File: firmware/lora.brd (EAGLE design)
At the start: 20.2 x 71.1 mm, 24 parts, among them J1 SWD_PTH_SHROUD, X1 SMA-142-0701-801/806

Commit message: some nudging
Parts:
- removed U$5: BUS-SMA, Ava:BUS-SMA
- moved X1 5.38 mm to (10.2, 0.76)
- moved J1 1.27 mm to (2.54, 55.9)
- moved U$1 1.27 mm to (10.2, 34.3)
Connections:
- net GND: no longer U$5.2, U$5.3, U$5.4, U$5.5
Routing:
- net RST: track 38.0 -> 27.6 mm
- net SWCLK: track 25.9 -> 20.3 mm
- net N$2: track 8.12 -> 12.9 mm
- net GND: track 171.4 -> 168.1 mm
- net SWDAT: track 23.3 -> 20.6 mm
- net N$4: track 57.7 -> 56.5 mm
- net +3V3: track 100.1 -> 99.5 mm
- net GPIO3: track 21.3 -> 20.8 mm
- added copper zone on layer 1, net GND

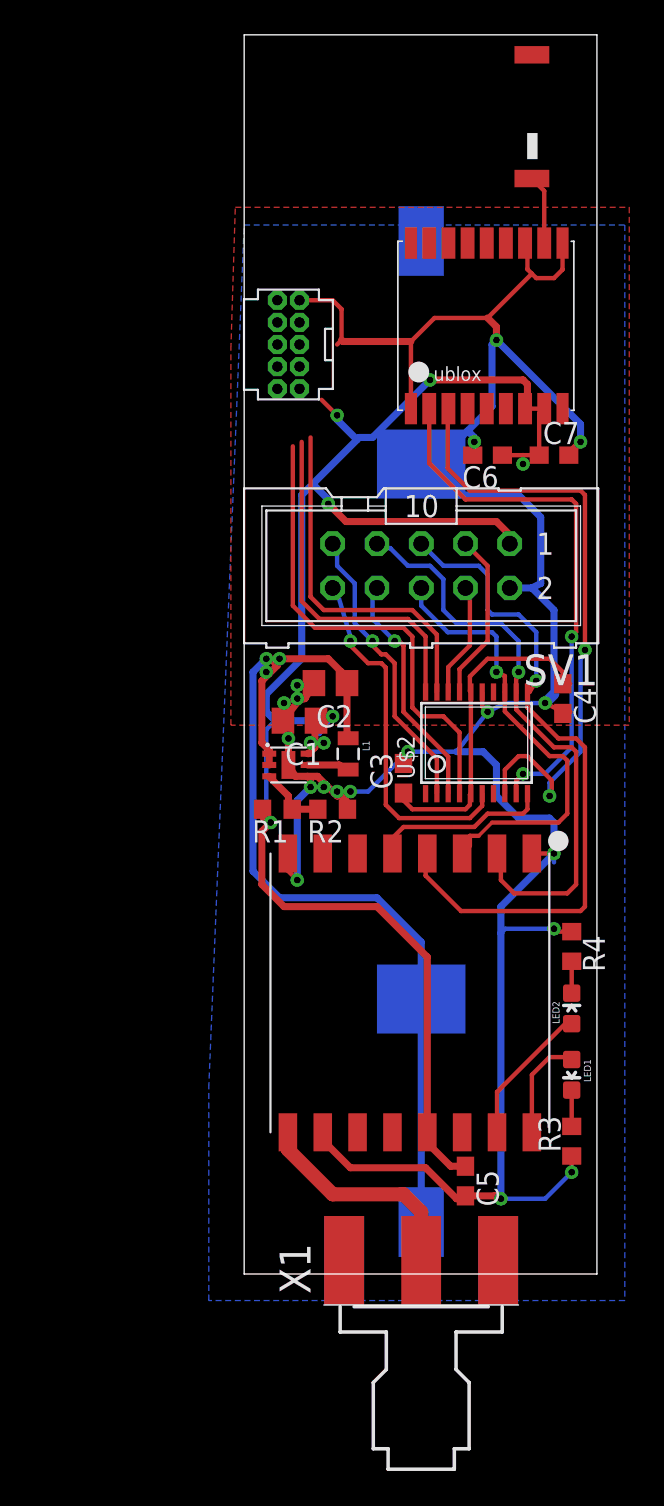
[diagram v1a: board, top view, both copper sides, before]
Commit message: added esd diodes and supply reading
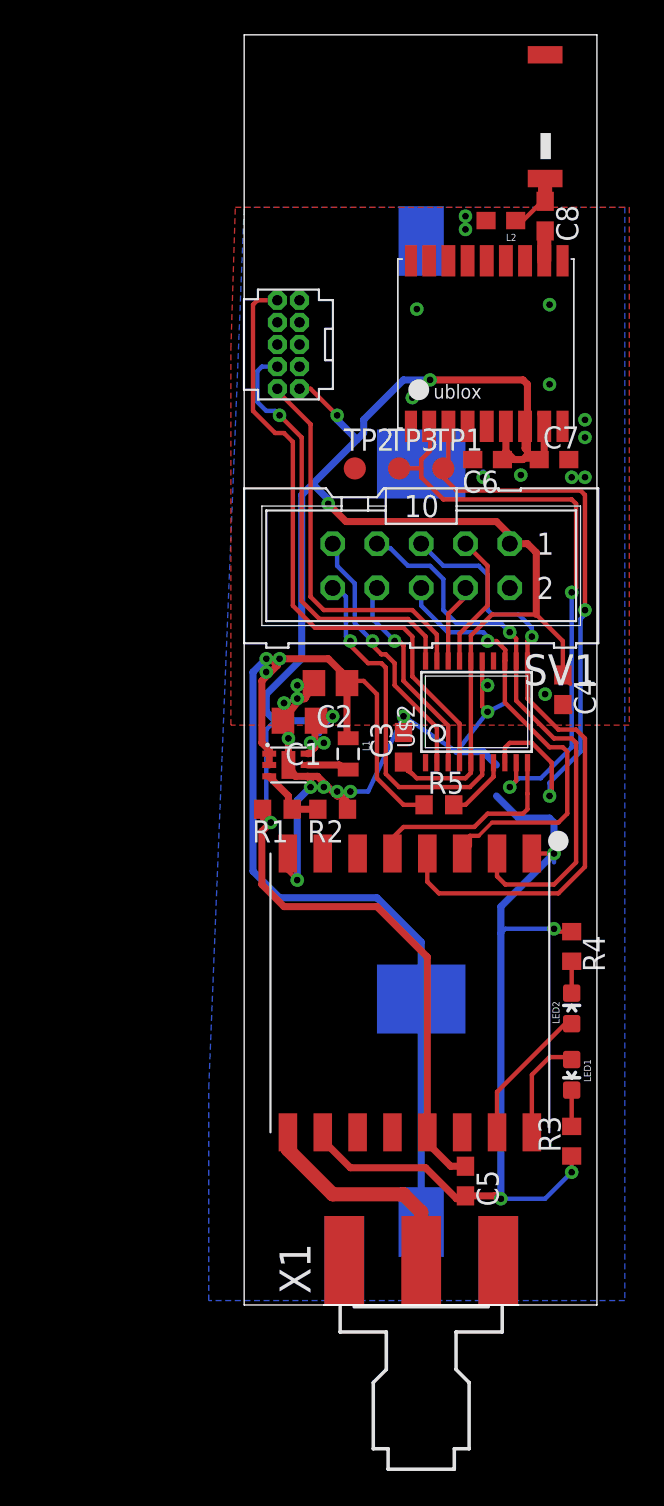
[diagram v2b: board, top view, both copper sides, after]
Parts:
- added C8: (no value), rcl:C0603
- added L2: (no value), SparkFun-Passives:0603
- added R5: (no value), rcl:R0603
- added TP1, TP2, TP3: PTR1B1,27, testpad:B1,27
- moved C3 1.78 mm to (9.14, 32.8)
- moved U$2 1.78 mm to (13.3, 34.8)
- moved U$3 1.02 mm to (14.0, 56.1)
- moved U$4 0.76 mm to (17.3, 68.6)
- moved C4 0.51 mm to (18.3, 36.1)
- moved C6 0.25 mm to (14.0, 49.3)
- moved C7 0.25 mm to (17.8, 49.3)
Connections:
- removed net N$11: C3.1, C4.1, U$2.16, U$2.5
- new net N$9: R5.2, U$2.7
- new net VBAT: C2.1, L1.1, R5.1, U$1.P1, U$1.P2, U$7.1, U$7.2
- net +3V3: now also C3.1, C4.1, U$2.16, U$2.5, U$3.6_V_BCKP
- net GND: now also L2.2, TP2.TP
- net N$1: now also C8.2; no longer U$4.FEED
- net N$4: now also C8.1, L2.1, U$4.FEED; no longer C2.1, L1.1, U$1.P1, U$1.P2, U$7.1, U$7.2
- net UART_RX: now also TP3.TP
- net UART_TX: now also TP1.TP
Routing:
- net GND: track 168.1 -> 95.3 mm, vias 19 -> 29
- net VBAT: track 0.00 -> 66.7 mm, vias 0 -> 3
- net N$4: track 56.5 -> 3.46 mm, vias 3 -> 0
- net +3V3: track 99.5 -> 133.1 mm, vias 8 -> 7
- net N$11: track 19.1 -> 0.00 mm
- net RST: track 27.6 -> 36.0 mm
- net SWCLK: track 20.3 -> 25.2 mm, vias 0 -> 1
- net N$9: track 0.00 -> 3.76 mm
- net UART_RX: track 31.3 -> 34.1 mm
- net SCLK: track 39.2 -> 36.9 mm
- net N$1: track 4.00 -> 1.73 mm
- net SWDAT: track 20.6 -> 22.4 mm
- net SDA: track 6.59 -> 4.81 mm
- net SCL: track 9.71 -> 7.93 mm
- net GPIO1: track 13.9 -> 12.1 mm
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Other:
- board size 20.2 x 71.1 mm -> 20.2 x 72.9 mm
